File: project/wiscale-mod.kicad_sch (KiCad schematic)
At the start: 47 parts, among them J1 TL, J2 TR, J3 BL, J4 BR, J5 cell, J6 DS18B20, J7 DS18B20, Q1 AO3401A, Q2 AO3401A, SW1 SW_SPDT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

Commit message: moving thermometer from D0 to D5. fixes #1
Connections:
- net 1w: now also U3.4 (SCK/D5); no longer U3.3 (D0)
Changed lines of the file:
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@@
   (no_connect (at 161.29 132.08))
   (no_connect (at 173.99 101.6))
-  (no_connect (at 161.29 124.46))
+  (no_connect (at 161.29 111.76))
   (wire (pts (xy 196.85 24.13) (xy 196.85 33.02))
     (stroke (width 0) (type default) (color 0 0 0 0))
@@
     (effects (font (size 0.3 0.3)) (justify left bottom))
   )
-  (label "1w" (at 161.29 111.76 180)
+  (label "1w" (at 161.29 124.46 180)
     (effects (font (size 1.27 1.27)) (justify right bottom))
   )

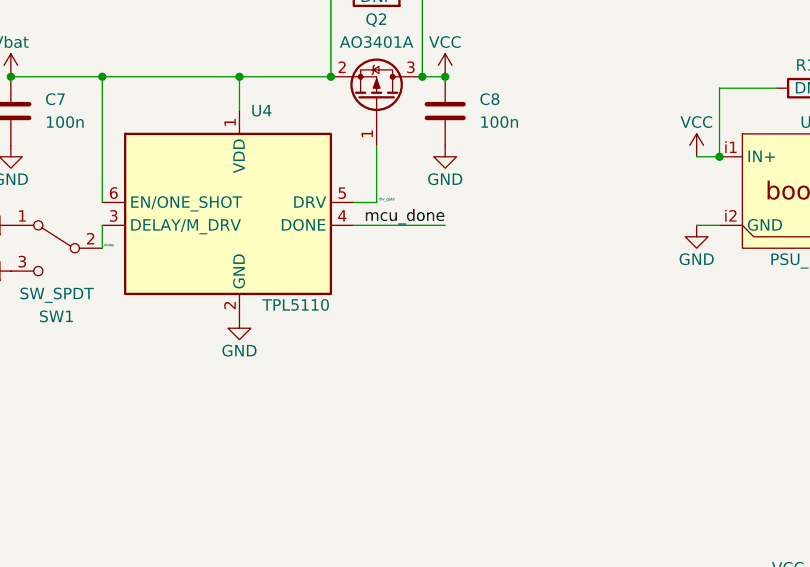
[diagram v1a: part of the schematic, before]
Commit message: adding pull-down on MCU_DONE pin. fixes #2
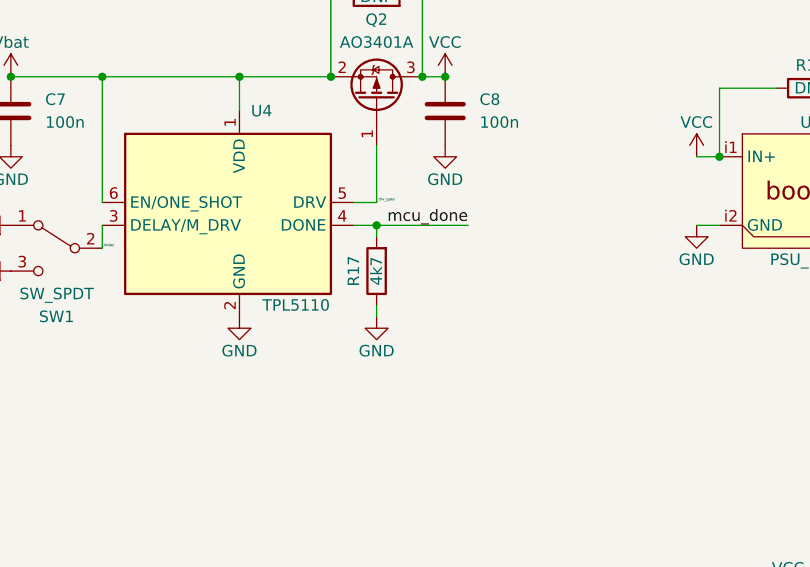
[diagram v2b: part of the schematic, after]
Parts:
- added R17: 4k7, Resistor_SMD:R_0805_2012Metric_Pad1.20x1.40mm_HandSolder, symbol Device:R
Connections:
- net GND: now also R17.1
- net mcu_done: now also R17.2
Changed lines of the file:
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@@
 (kicad_sch (version 20211123) (generator eeschema)
   (paper "A4")
+  (junction (at 201.93 49.53) (diameter 0) (color 0 0 0 0)
+  )
   (junction (at 80.01 123.19) (diameter 0) (color 0 0 0 0)
   )
@@
     (stroke (width 0) (type default) (color 0 0 0 0))
   )
+  (wire (pts (xy 201.93 50.8) (xy 201.93 49.53))
+    (stroke (width 0) (type default) (color 0 0 0 0))
+  )
   (wire (pts (xy 69.85 137.16) (xy 76.2 137.16))
     (stroke (width 0) (type default) (color 0 0 0 0))
@@
     (stroke (width 0) (type default) (color 0 0 0 0))
   )
+  (wire (pts (xy 201.93 59.69) (xy 201.93 58.42))
+    (stroke (width 0) (type default) (color 0 0 0 0))
+  )
   (wire (pts (xy 78.74 132.08) (xy 76.2 132.08))
     (stroke (width 0) (type default) (color 0 0 0 0))
@@
     (stroke (width 0) (type default) (color 0 0 0 0))
   )
-  (wire (pts (xy 199.39 49.53) (xy 209.55 49.53))
+  (wire (pts (xy 199.39 49.53) (xy 201.93 49.53))
     (stroke (width 0) (type default) (color 0 0 0 0))
   )
@@
   )
   (wire (pts (xy 80.01 123.19) (xy 90.17 123.19))
+    (stroke (width 0) (type default) (color 0 0 0 0))
+  )
+  (wire (pts (xy 201.93 49.53) (xy 212.09 49.53))
     (stroke (width 0) (type default) (color 0 0 0 0))
   )
@@
     (effects (font (size 1.27 1.27)) (justify left bottom))
   )
-  (label "mcu_done" (at 209.55 49.53 180)
+  (label "mcu_done" (at 212.09 49.53 180)
     (effects (font (size 1.27 1.27)) (justify right bottom))
   )
@@
     )
     (pin "1")
+  )
+  (symbol (lib_id "Device:R") (at 201.93 54.61 180) (unit 1)
+    (in_bom yes) (on_board yes)
+    (property "Reference" "R17" (id 0) (at 199.39 54.61 90))
+    (property "Value" "4k7" (id 1) (at 201.93 54.61 90))
+    (property "Footprint" "Resistor_SMD:R_0805_2012Metric_Pad1.20x1.40mm_HandSolder" (id 2) (at 203.708 54.61 90)
+      (effects (font (size 1.27 1.27)) hide)
+    )
+    (property "Datasheet" "~" (id 3) (at 201.93 54.61 0)
+      (effects (font (size 1.27 1.27)) hide)
+    )
+    (pin "1")
+    (pin "2")
   )
   (symbol (lib_id "Connector_Generic_MountingPin:Conn_01x04_MountingPin") (at 71.12 160.02 0) (mirror y) (unit 1)
@@
     (pin "1")
     (pin "2")
+  )
+  (symbol (lib_id "power:GND") (at 201.93 59.69 0) (unit 1)
+    (in_bom yes) (on_board yes)
+    (property "Reference" "#PWR034" (id 0) (at 201.93 66.04 0)
+      (effects (font (size 1.27 1.27)) hide)
+    )
+    (property "Value" "GND" (id 1) (at 201.93 63.5 0))
+    (property "Footprint" "" (id 2) (at 201.93 59.69 0)
+      (effects (font (size 1.27 1.27)) hide)
+    )
+    (property "Datasheet" "" (id 3) (at 201.93 59.69 0)
+      (effects (font (size 1.27 1.27)) hide)
+    )
+    (pin "1")
   )
   (symbol (lib_id "Device:R") (at 201.93 24.13 90) (unit 1)
@@
       (reference "#PWR033") (unit 1) (value "GND") (footprint "")
     )
+    (path "/2039d43f-d36d-4b5f-b1ad-fcba316c9644"
+      (reference "#PWR034") (unit 1) (value "GND") (footprint "")
+    )
     (path "/bb6e4d2c-b491-48c4-ab7d-2d534a80636a"
       (reference "BT1") (unit 1) (value "LiPo") (footprint "-local:BAT_BH-18650-PC")
@@
       (reference "R16") (unit 1) (value "DNP") (footprint "Resistor_SMD:R_0805_2012Metric_Pad1.20x1.40mm_HandSolder")
     )
+    (path "/16075b09-deb0-4bf2-8909-c66f62369c80"
+      (reference "R17") (unit 1) (value "4k7") (footprint "Resistor_SMD:R_0805_2012Metric_Pad1.20x1.40mm_HandSolder")
+    )
     (path "/7de5144c-6ce8-430c-b738-ec801808f61d"

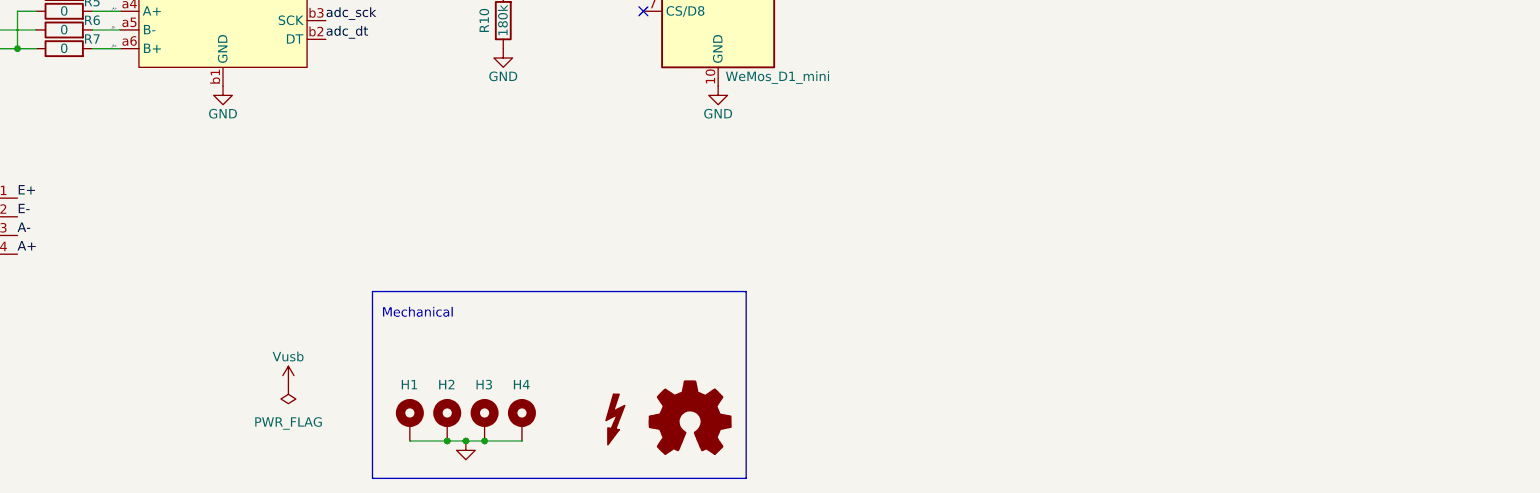
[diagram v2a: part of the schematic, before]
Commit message: adding caps to ADC input to average out noise
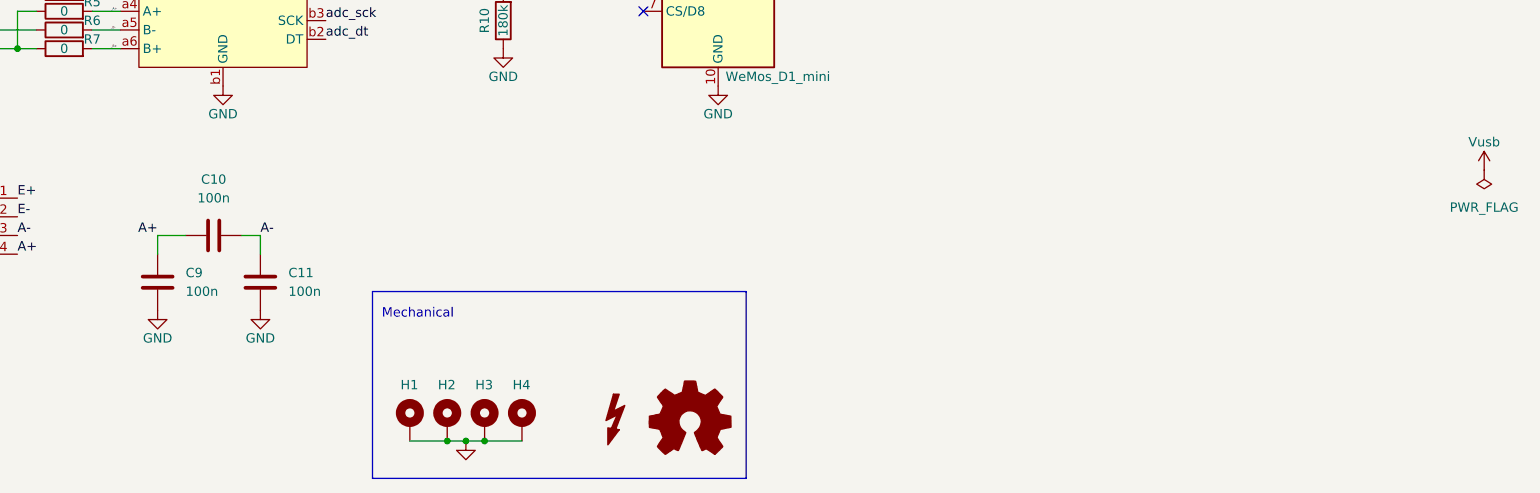
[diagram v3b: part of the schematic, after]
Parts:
- added C10, C11, C9: 100n, Capacitor_SMD:C_0805_2012Metric_Pad1.18x1.45mm_HandSolder, symbol Device:C
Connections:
- net A+: now also C10.2, C9.2
- net A-: now also C10.1, C11.2
- net GND: now also C11.1, C9.1
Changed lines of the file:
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@@
+    (stroke (width 0) (type default) (color 0 0 0 0))
+  )
+  (wire (pts (xy 106.68 162.56) (xy 109.22 162.56))
     (stroke (width 0) (type default) (color 0 0 0 0))
   )
@@
     (stroke (width 0) (type default) (color 0 0 0 0))
   )
+  (wire (pts (xy 95.25 162.56) (xy 99.06 162.56))
+    (stroke (width 0) (type default) (color 0 0 0 0))
+  )
   (wire (pts (xy 109.22 36.83) (xy 118.11 36.83))
     (stroke (width 0) (type default) (color 0 0 0 0))
@@
     (stroke (width 0) (type default) (color 0 0 0 0))
   )
+  (wire (pts (xy 95.25 165.1) (xy 95.25 162.56))
+    (stroke (width 0) (type default) (color 0 0 0 0))
+  )
   (wire (pts (xy 199.39 46.99) (xy 201.93 46.99))
     (stroke (width 0) (type default) (color 0 0 0 0))
@@
   )
   (wire (pts (xy 158.75 109.22) (xy 161.29 109.22))
+    (stroke (width 0) (type default) (color 0 0 0 0))
+  )
+  (wire (pts (xy 109.22 162.56) (xy 109.22 165.1))
     (stroke (width 0) (type default) (color 0 0 0 0))
   )
@@
     (effects (font (size 1.27 1.27)) (justify left bottom))
   )
+  (label "A+" (at 95.25 162.56 180)
+    (effects (font (size 1.27 1.27)) (justify right bottom))
+  )
   (label "_A+" (at 88.9 132.08 0)
     (effects (font (size 0.3 0.3)) (justify left bottom))
@@
   )
   (label "E-" (at 76.2 160.02 0)
+    (effects (font (size 1.27 1.27)) (justify left bottom))
+  )
+  (label "A-" (at 109.22 162.56 0)
     (effects (font (size 1.27 1.27)) (justify left bottom))
   )
@@
     (pin "2")
   )
+  (symbol (lib_id "Device:C") (at 109.22 168.91 180) (unit 1)
+    (in_bom yes) (on_board yes) (fields_autoplaced)
+    (property "Reference" "C11" (id 0) (at 113.03 167.6399 0)
+      (effects (font (size 1.27 1.27)) (justify right))
+    )
+    (property "Value" "100n" (id 1) (at 113.03 170.1799 0)
+      (effects (font (size 1.27 1.27)) (justify right))
+    )
+    (property "Footprint" "Capacitor_SMD:C_0805_2012Metric_Pad1.18x1.45mm_HandSolder" (id 2) (at 108.2548 165.1 0)
+      (effects (font (size 1.27 1.27)) hide)
+    )
+    (property "Datasheet" "~" (id 3) (at 109.22 168.91 0)
+      (effects (font (size 1.27 1.27)) hide)
+    )
+    (pin "1")
+    (pin "2")
+  )
   (symbol (lib_id "Device:C") (at 209.55 36.83 180) (unit 1)
     (in_bom yes) (on_board yes) (fields_autoplaced)
@@
     (pin "2")
   )
-  (symbol (lib_id "power:PWR_FLAG") (at 113.03 182.88 180) (unit 1)
+  (symbol (lib_id "power:PWR_FLAG") (at 275.59 153.67 180) (unit 1)
     (in_bom yes) (on_board yes) (fields_autoplaced)
-    (property "Reference" "#FLG01" (id 0) (at 113.03 184.785 0)
-      (effects (font (size 1.27 1.27)) hide)
-    )
-    (property "Value" "PWR_FLAG" (id 1) (at 113.03 187.96 0))
-    (property "Footprint" "" (id 2) (at 113.03 182.88 0)
-      (effects (font (size 1.27 1.27)) hide)
-    )
-    (property "Datasheet" "~" (id 3) (at 113.03 182.88 0)
+    (property "Reference" "#FLG01" (id 0) (at 275.59 155.575 0)
+      (effects (font (size 1.27 1.27)) hide)
+    )
+    (property "Value" "PWR_FLAG" (id 1) (at 275.59 158.75 0))
+    (property "Footprint" "" (id 2) (at 275.59 153.67 0)
+      (effects (font (size 1.27 1.27)) hide)
+    )
+    (property "Datasheet" "~" (id 3) (at 275.59 153.67 0)
       (effects (font (size 1.27 1.27)) hide)
     )
@@
     (pin "o1")
     (pin "o2")
+  )
+  (symbol (lib_id "power:GND") (at 95.25 172.72 0) (unit 1)
+    (in_bom yes) (on_board yes)
+    (property "Reference" "#PWR035" (id 0) (at 95.25 179.07 0)
+      (effects (font (size 1.27 1.27)) hide)
+    )
+    (property "Value" "GND" (id 1) (at 95.25 176.53 0))
+    (property "Footprint" "" (id 2) (at 95.25 172.72 0)
+      (effects (font (size 1.27 1.27)) hide)
+    )
+    (property "Datasheet" "" (id 3) (at 95.25 172.72 0)
+      (effects (font (size 1.27 1.27)) hide)
+    )
+    (pin "1")
   )
   (symbol (lib_id "MCU_Module:WeMos_D1_mini") (at 171.45 121.92 0) (mirror y) (unit 1)
@@
     (pin "T")
   )
-  (symbol (lib_id "-pwr:Vusb") (at 113.03 182.88 0) (unit 1)
-    (in_bom yes) (on_board yes)
-    (property "Reference" "#PWR015" (id 0) (at 113.03 186.69 0)
-      (effects (font (size 1.27 1.27)) hide)
-    )
-    (property "Value" "Vusb" (id 1) (at 113.03 179.07 0))
-    (property "Footprint" "" (id 2) (at 113.03 182.88 0)
-      (effects (font (size 1.27 1.27)) hide)
-    )
-    (property "Datasheet" "" (id 3) (at 113.03 182.88 0)
+  (symbol (lib_id "-pwr:Vusb") (at 275.59 153.67 0) (unit 1)
+    (in_bom yes) (on_board yes)
+    (property "Reference" "#PWR015" (id 0) (at 275.59 157.48 0)
+      (effects (font (size 1.27 1.27)) hide)
+    )
+    (property "Value" "Vusb" (id 1) (at 275.59 149.86 0))
+    (property "Footprint" "" (id 2) (at 275.59 153.67 0)
+      (effects (font (size 1.27 1.27)) hide)
+    )
+    (property "Datasheet" "" (id 3) (at 275.59 153.67 0)
       (effects (font (size 1.27 1.27)) hide)
     )
@@
       (effects (font (size 1.27 1.27)) hide)
     )
+  )
+  (symbol (lib_id "Device:C") (at 95.25 168.91 180) (unit 1)
+    (in_bom yes) (on_board yes) (fields_autoplaced)
+    (property "Reference" "C9" (id 0) (at 99.06 167.6399 0)
+      (effects (font (size 1.27 1.27)) (justify right))
+    )
+    (property "Value" "100n" (id 1) (at 99.06 170.1799 0)
+      (effects (font (size 1.27 1.27)) (justify right))
+    )
+    (property "Footprint" "Capacitor_SMD:C_0805_2012Metric_Pad1.18x1.45mm_HandSolder" (id 2) (at 94.2848 165.1 0)
+      (effects (font (size 1.27 1.27)) hide)
+    )
+    (property "Datasheet" "~" (id 3) (at 95.25 168.91 0)
+      (effects (font (size 1.27 1.27)) hide)
+    )
+    (pin "1")
+    (pin "2")
   )
   (symbol (lib_id "Device:Battery_Cell") (at 100.33 40.64 90) (unit 1)
@@
     (pin "2")
   )
+  (symbol (lib_id "power:GND") (at 109.22 172.72 0) (unit 1)
+    (in_bom yes) (on_board yes)
+    (property "Reference" "#PWR036" (id 0) (at 109.22 179.07 0)
+      (effects (font (size 1.27 1.27)) hide)
+    )
+    (property "Value" "GND" (id 1) (at 109.22 176.53 0))
+    (property "Footprint" "" (id 2) (at 109.22 172.72 0)
+      (effects (font (size 1.27 1.27)) hide)
+    )
+    (property "Datasheet" "" (id 3) (at 109.22 172.72 0)
+      (effects (font (size 1.27 1.27)) hide)
+    )
+    (pin "1")
+  )
+  (symbol (lib_id "Device:C") (at 102.87 162.56 270) (unit 1)
+    (in_bom yes) (on_board yes) (fields_autoplaced)
+    (property "Reference" "C10" (id 0) (at 102.87 154.94 90))
+    (property "Value" "100n" (id 1) (at 102.87 157.48 90))
+    (property "Footprint" "Capacitor_SMD:C_0805_2012Metric_Pad1.18x1.45mm_HandSolder" (id 2) (at 99.06 163.5252 0)
+      (effects (font (size 1.27 1.27)) hide)
+    )
+    (property "Datasheet" "~" (id 3) (at 102.87 162.56 0)
+      (effects (font (size 1.27 1.27)) hide)
+    )
+    (pin "1")
+    (pin "2")
+  )
   (symbol (lib_id "power:GND") (at 26.67 179.07 0) (unit 1)
     (in_bom yes) (on_board yes)
@@
       (reference "#PWR034") (unit 1) (value "GND") (footprint "")
     )
+    (path "/8143fa17-0dfe-40b2-a1cc-4505c9ead310"
+      (reference "#PWR035") (unit 1) (value "GND") (footprint "")
+    )
+    (path "/d7e2c21c-941a-4520-ad1f-ab94d3c20eed"
+      (reference "#PWR036") (unit 1) (value "GND") (footprint "")
+    )
     (path "/bb6e4d2c-b491-48c4-ab7d-2d534a80636a"
       (reference "BT1") (unit 1) (value "LiPo") (footprint "-local:BAT_BH-18650-PC")
@@
       (reference "C8") (unit 1) (value "100n") (footprint "Capacitor_SMD:C_0805_2012Metric_Pad1.18x1.45mm_HandSolder")
     )
+    (path "/b3f202b6-7e36-4306-b99b-7f535cf911b1"
+      (reference "C9") (unit 1) (value "100n") (footprint "Capacitor_SMD:C_0805_2012Metric_Pad1.18x1.45mm_HandSolder")
+    )
+    (path "/d9277dbd-542d-46d5-b241-4ee6378e2272"
+      (reference "C10") (unit 1) (value "100n") (footprint "Capacitor_SMD:C_0805_2012Metric_Pad1.18x1.45mm_HandSolder")
+    )
+    (path "/57534cb9-a031-4952-8de9-bb0a8e09acaa"
+      (reference "C11") (unit 1) (value "100n") (footprint "Capacitor_SMD:C_0805_2012Metric_Pad1.18x1.45mm_HandSolder")
+    )
     (path "/7853fe60-ab7e-4260-ae97-5e83ebb81ab7"
